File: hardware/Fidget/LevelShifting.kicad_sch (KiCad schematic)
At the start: 20 parts

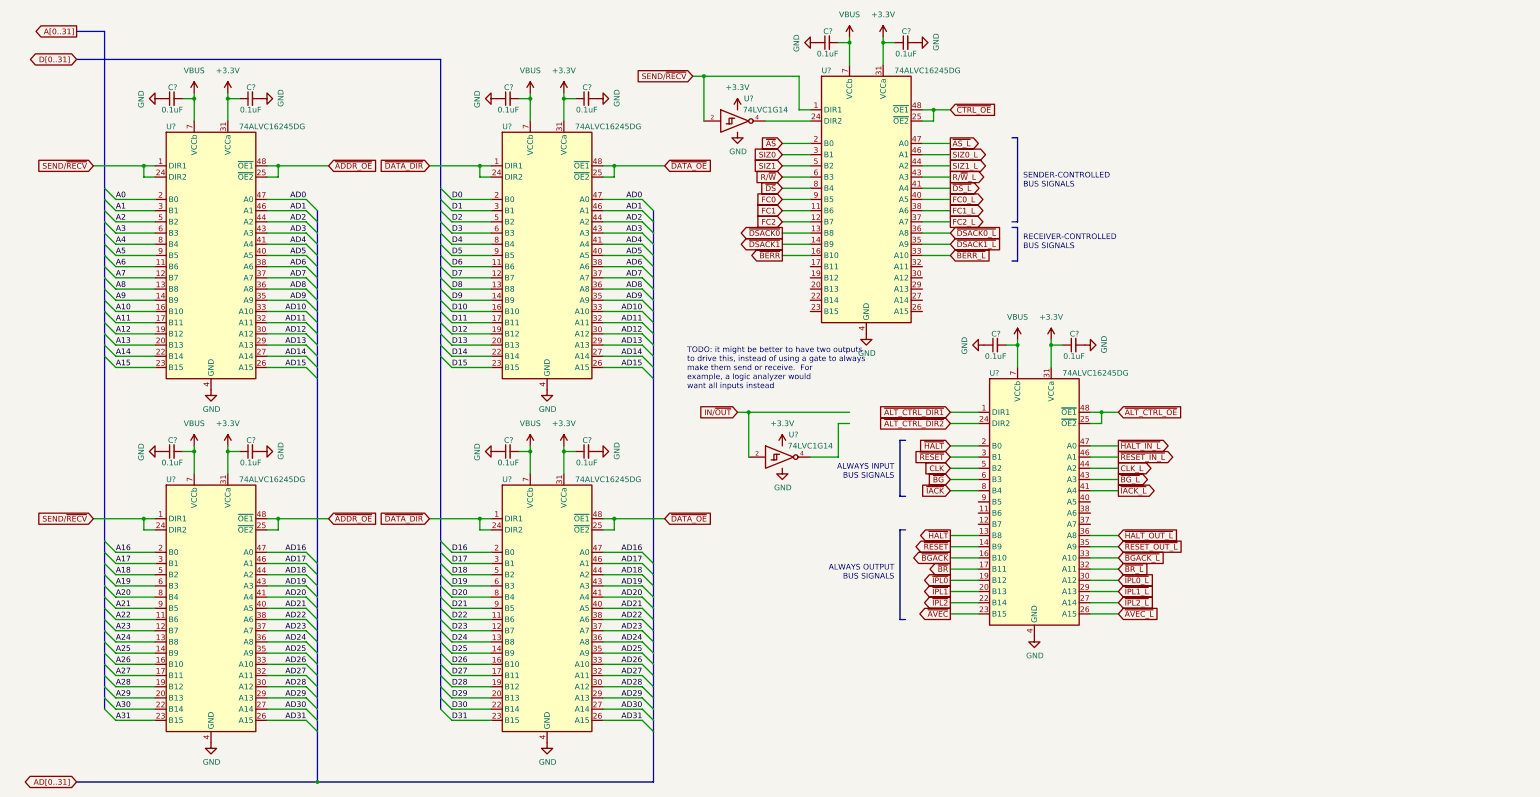
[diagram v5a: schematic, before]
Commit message: Minor updates, and start of PCB layout
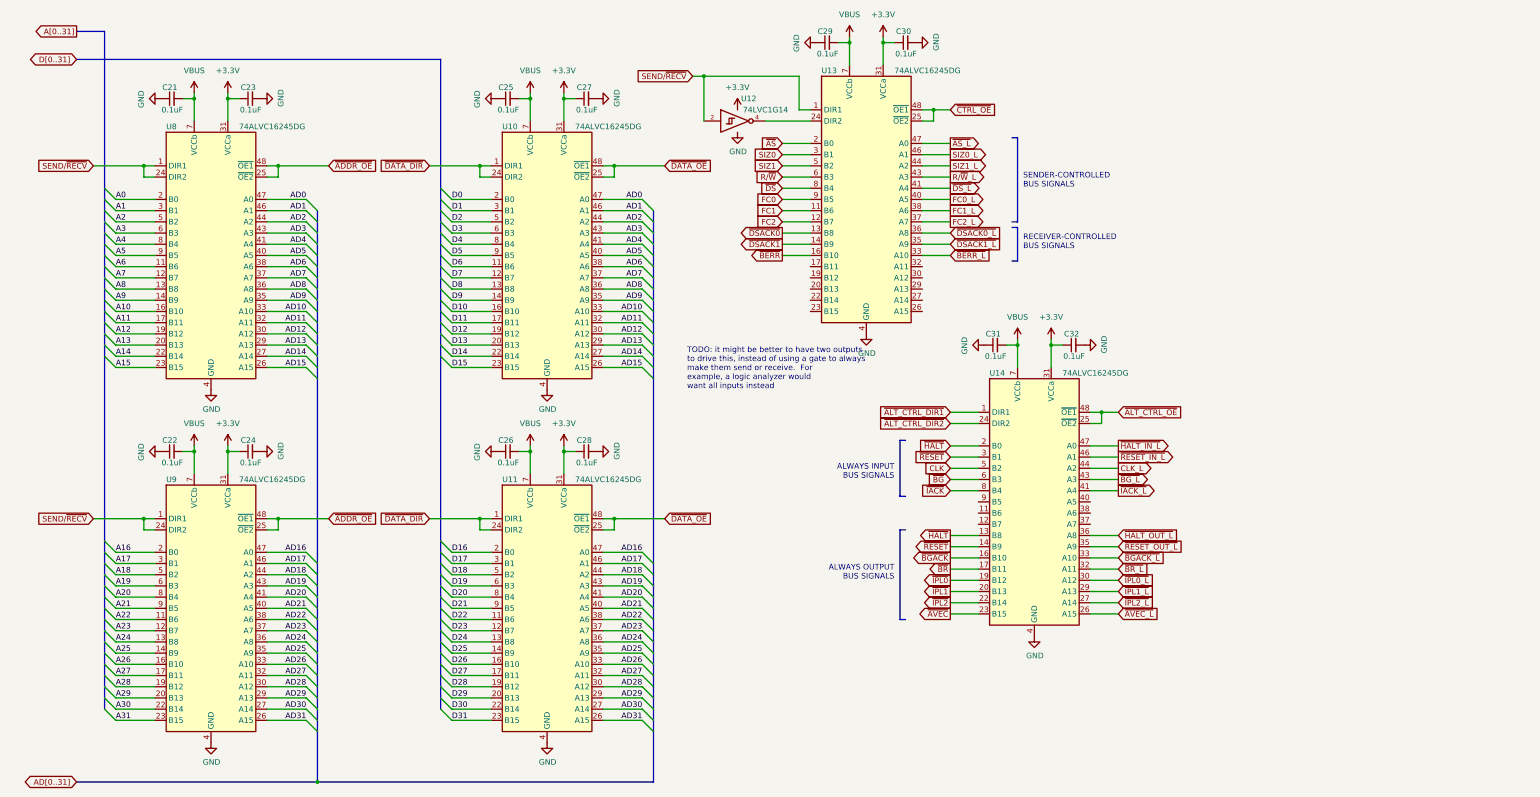
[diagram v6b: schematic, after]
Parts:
- removed U?: 74LVC1G14, symbol 74xGxx:74LVC1G14
- C21, C22, C23, C24, C25, C26, C27, C28, C29, C30, C31, C32: renamed from C?; footprint (none) -> Capacitor_SMD:C_0805_2012Metric_Pad1.18x1.45mm_HandSolder
- U12: renamed from U?; footprint (none) -> Package_TO_SOT_SMD:SOT-353_SC-70-5_Handsoldering
- gave numbers to parts that had none: 6

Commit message: Almost done Rev1 board design
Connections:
- no-connect marks 0 -> 16
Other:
- note removed: "TODO: it might be better to have two outputs to drive this, instead of using a gate to always make them send or receive. For example, a logic analyzer would want all inputs instead"
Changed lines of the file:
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@@
 (kicad_sch (version 20211123) (generator eeschema)
   (paper "A4")
+  (junction (at 203.2 22.86) (diameter 0) (color 0 0 0 0)
+  )
   (junction (at 170.18 30.48) (diameter 0) (color 0 0 0 0)
   )
+  (junction (at 130.81 35.56) (diameter 0) (color 0 0 0 0)
+  )
   (junction (at 43.18 50.8) (diameter 0) (color 0 0 0 0)
   )
@@
   (junction (at 73.66 50.8) (diameter 0) (color 0 0 0 0)
   )
-  (junction (at 203.2 22.86) (diameter 0) (color 0 0 0 0)
-  )
   (junction (at 62.23 115.57) (diameter 0) (color 0 0 0 0)
   )
@@
   (junction (at 222.25 38.1) (diameter 0) (color 0 0 0 0)
   )
-  (junction (at 130.81 35.56) (diameter 0) (color 0 0 0 0)
-  )
   (junction (at 54.61 35.56) (diameter 0) (color 0 0 0 0)
   )
@@
   (junction (at 82.55 190.5) (diameter 0) (color 0 0 0 0)
   )
+  (no_connect (at 194.31 73.66))
+  (no_connect (at 219.71 78.74))
+  (no_connect (at 219.71 83.82))
+  (no_connect (at 257.81 127))
+  (no_connect (at 194.31 83.82))
+  (no_connect (at 194.31 81.28))
+  (no_connect (at 232.41 127))
+  (no_connect (at 219.71 81.28))
+  (no_connect (at 194.31 78.74))
+  (no_connect (at 257.81 129.54))
+  (no_connect (at 219.71 76.2))
+  (no_connect (at 232.41 132.08))
+  (no_connect (at 194.31 76.2))
+  (no_connect (at 257.81 132.08))
+  (no_connect (at 219.71 73.66))
+  (no_connect (at 232.41 129.54))
   (bus_entry (at 36.83 91.44) (size -2.54 -2.54)
     (stroke (width 0) (type default) (color 0 0 0 0))
@@
     (stroke (width 0) (type default) (color 0 0 0 0))
   )
-  (wire (pts (xy 203.2 22.86) (xy 203.2 27.94))
-    (stroke (width 0) (type default) (color 0 0 0 0))
-  )
   (wire (pts (xy 71.12 148.59) (xy 80.01 148.59))
     (stroke (width 0) (type default) (color 0 0 0 0))
@@
     (stroke (width 0) (type default) (color 0 0 0 0))
   )
+  (wire (pts (xy 200.66 22.86) (xy 203.2 22.86))
+    (stroke (width 0) (type default) (color 0 0 0 0))
+  )
   (wire (pts (xy 36.83 158.75) (xy 45.72 158.75))
     (stroke (width 0) (type default) (color 0 0 0 0))
@@
     (stroke (width 0) (type default) (color 0 0 0 0))
   )
-  (wire (pts (xy 203.2 21.59) (xy 203.2 22.86))
-    (stroke (width 0) (type default) (color 0 0 0 0))
-  )
   (wire (pts (xy 71.12 86.36) (xy 80.01 86.36))
     (stroke (width 0) (type default) (color 0 0 0 0))
@@
     (stroke (width 0) (type default) (color 0 0 0 0))
   )
+  (wire (pts (xy 128.27 35.56) (xy 130.81 35.56))
+    (stroke (width 0) (type default) (color 0 0 0 0))
+  )
   (polyline (pts (xy 241.3 64.77) (xy 241.3 72.39))
     (stroke (width 0) (type solid) (color 0 0 0 0))
@@
     (stroke (width 0) (type default) (color 0 0 0 0))
   )
-  (wire (pts (xy 130.81 35.56) (xy 130.81 40.64))
-    (stroke (width 0) (type default) (color 0 0 0 0))
-  )
   (polyline (pts (xy 240.03 44.45) (xy 241.3 44.45))
     (stroke (width 0) (type solid) (color 0 0 0 0))
@@
     (stroke (width 0) (type default) (color 0 0 0 0))
   )
-  (wire (pts (xy 128.27 35.56) (xy 130.81 35.56))
-    (stroke (width 0) (type default) (color 0 0 0 0))
-  )
   (bus (pts (xy 110.49 26.67) (xy 110.49 55.88))
     (stroke (width 0) (type default) (color 0 0 0 0))
@@
     (stroke (width 0) (type default) (color 0 0 0 0))
   )
+  (wire (pts (xy 130.81 35.56) (xy 130.81 40.64))
+    (stroke (width 0) (type default) (color 0 0 0 0))
+  )
   (wire (pts (xy 71.12 153.67) (xy 80.01 153.67))
     (stroke (width 0) (type default) (color 0 0 0 0))
@@
     (stroke (width 0) (type default) (color 0 0 0 0))
   )
+  (wire (pts (xy 130.81 34.29) (xy 130.81 35.56))
+    (stroke (width 0) (type default) (color 0 0 0 0))
+  )
   (wire (pts (xy 219.71 45.72) (xy 226.06 45.72))
     (stroke (width 0) (type default) (color 0 0 0 0))
@@
     (stroke (width 0) (type default) (color 0 0 0 0))
   )
-  (wire (pts (xy 130.81 34.29) (xy 130.81 35.56))
-    (stroke (width 0) (type default) (color 0 0 0 0))
-  )
   (wire (pts (xy 45.72 91.44) (xy 36.83 91.44))
     (stroke (width 0) (type default) (color 0 0 0 0))
@@
     (stroke (width 0) (type default) (color 0 0 0 0))
   )
+  (wire (pts (xy 203.2 22.86) (xy 203.2 27.94))
+    (stroke (width 0) (type default) (color 0 0 0 0))
+  )
   (wire (pts (xy 45.72 168.91) (xy 36.83 168.91))
     (stroke (width 0) (type default) (color 0 0 0 0))
@@
     (stroke (width 0) (type default) (color 0 0 0 0))
   )
-  (wire (pts (xy 200.66 22.86) (xy 203.2 22.86))
-    (stroke (width 0) (type default) (color 0 0 0 0))
-  )
   (bus (pts (xy 82.55 66.04) (xy 82.55 68.58))
     (stroke (width 0) (type default) (color 0 0 0 0))
@@
     (stroke (width 0) (type default) (color 0 0 0 0))
   )
-  (wire (pts (xy 147.32 81.28) (xy 156.21 81.28))
+  (wire (pts (xy 203.2 21.59) (xy 203.2 22.86))
     (stroke (width 0) (type default) (color 0 0 0 0))
   )
-  (text "TODO: it might be better to have two outputs\nto drive this, instead of using a gate to always\nmake them send or receive.  For\nexample, a logic analyzer would\nwant all inputs instead"
-    (at 166.37 101.6 0)
-    (effects (font (size 1.27 1.27)) (justify left bottom))
+  (wire (pts (xy 147.32 81.28) (xy 156.21 81.28))
+    (stroke (width 0) (type default) (color 0 0 0 0))
   )
   (text "SENDER-CONTROLLED\nBUS SIGNALS\n" (at 242.57 55.88 0)
@@
     (pin "1")
   )
-  (symbol (lib_id "power:VBUS") (at 203.2 21.59 0) (unit 1)
-    (in_bom yes) (on_board yes) (fields_autoplaced)
-    (property "Reference" "#PWR092" (id 0) (at 203.2 25.4 0)
-      (effects (font (size 1.27 1.27)) hide)
-    )
-    (property "Value" "VBUS" (id 1) (at 203.2 16.51 0))
-    (property "Footprint" "" (id 2) (at 203.2 21.59 0)
-      (effects (font (size 1.27 1.27)) hide)
-    )
-    (property "Datasheet" "" (id 3) (at 203.2 21.59 0)
-      (effects (font (size 1.27 1.27)) hide)
-    )
-    (pin "1")
-  )
   (symbol (lib_id "Device:C_Small") (at 125.73 35.56 90) (unit 1)
     (in_bom yes) (on_board yes)
@@
     (pin "1")
   )
+  (symbol (lib_id "power:VBUS") (at 203.2 21.59 0) (unit 1)
+    (in_bom yes) (on_board yes) (fields_autoplaced)
+    (property "Reference" "#PWR0119" (id 0) (at 203.2 25.4 0)
+      (effects (font (size 1.27 1.27)) hide)
+    )
+    (property "Value" "VBUS" (id 1) (at 203.2 16.51 0))
+    (property "Footprint" "" (id 2) (at 203.2 21.59 0)
+      (effects (font (size 1.27 1.27)) hide)
+    )
+    (property "Datasheet" "" (id 3) (at 203.2 21.59 0)
+      (effects (font (size 1.27 1.27)) hide)
+    )
+    (pin "1")
+  )
   (symbol (lib_id "power:GND") (at 46.99 115.57 270) (unit 1)
     (in_bom yes) (on_board yes)
@@
     (pin "1")
   )
+  (symbol (lib_id "power:VBUS") (at 130.81 34.29 0) (unit 1)
+    (in_bom yes) (on_board yes) (fields_autoplaced)
+    (property "Reference" "#PWR0120" (id 0) (at 130.81 38.1 0)
+      (effects (font (size 1.27 1.27)) hide)
+    )
+    (property "Value" "VBUS" (id 1) (at 130.81 29.21 0))
+    (property "Footprint" "" (id 2) (at 130.81 34.29 0)
+      (effects (font (size 1.27 1.27)) hide)
+    )
+    (property "Datasheet" "" (id 3) (at 130.81 34.29 0)
+      (effects (font (size 1.27 1.27)) hide)
+    )
+    (pin "1")
+  )
   (symbol (lib_id "Fidget:74ALVC16245DG") (at 134.62 151.13 0) (unit 1)
     (in_bom yes) (on_board yes)
@@
       (effects (font (size 1.27 1.27)) hide)
     )
-    (pin "1")
-  )
-  (symbol (lib_id "power:VBUS") (at 130.81 34.29 0) (unit 1)
-    (in_bom yes) (on_board yes) (fields_autoplaced)
-    (property "Reference" "#PWR081" (id 0) (at 130.81 38.1 0)
-      (effects (font (size 1.27 1.27)) hide)
-    )
-    (property "Value" "VBUS" (id 1) (at 130.81 29.21 0))
-    (property "Footprint" "" (id 2) (at 130.81 34.29 0)
-      (effects (font (size 1.27 1.27)) hide)
-    )
-    (property "Datasheet" "" (id 3) (at 130.81 34.29 0)
-      (effects (font (size 1.27 1.27)) hide)
-    )
